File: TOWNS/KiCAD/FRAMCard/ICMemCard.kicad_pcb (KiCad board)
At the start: 2 copper layers, 79.1 x 50.5 mm, 17 parts, among them J1 PCMCIA_Connector, Q1 BC846X, Q2 BC846X, U1 FM18W08-SGTR, U2 FM18W08-SGTR

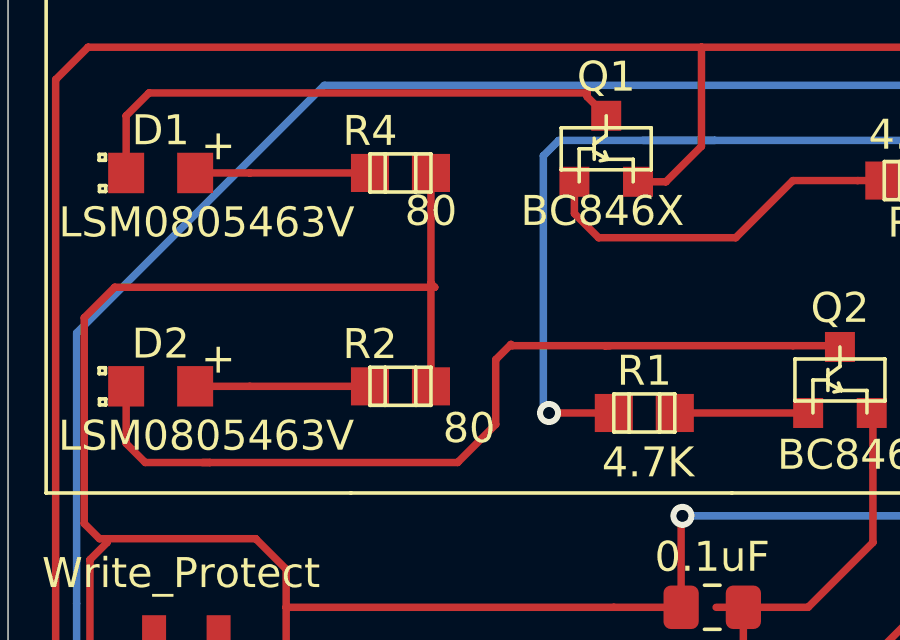
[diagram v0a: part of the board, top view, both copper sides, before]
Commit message: Updated resistance.
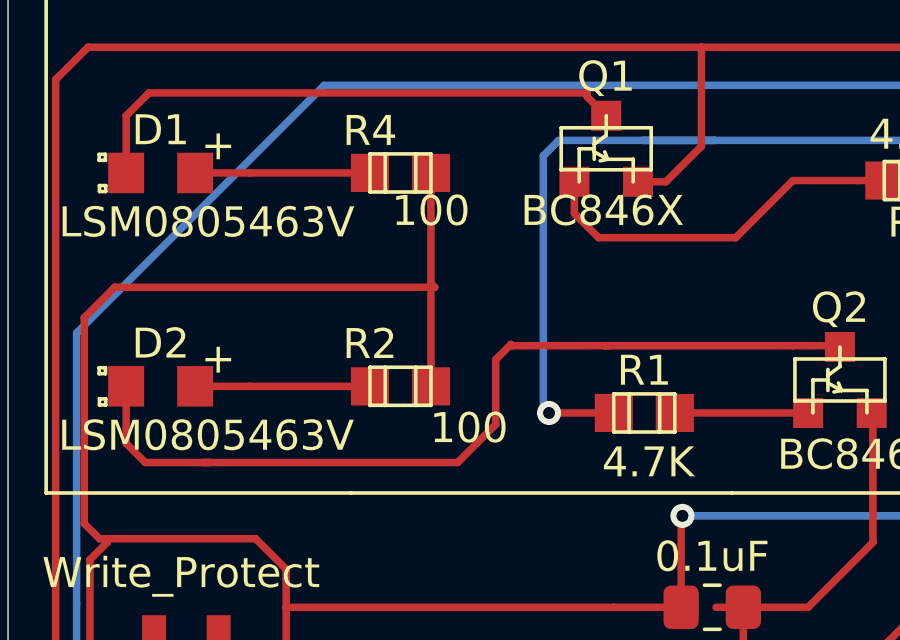
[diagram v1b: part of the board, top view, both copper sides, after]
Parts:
- R2, R4: value 80 -> 100

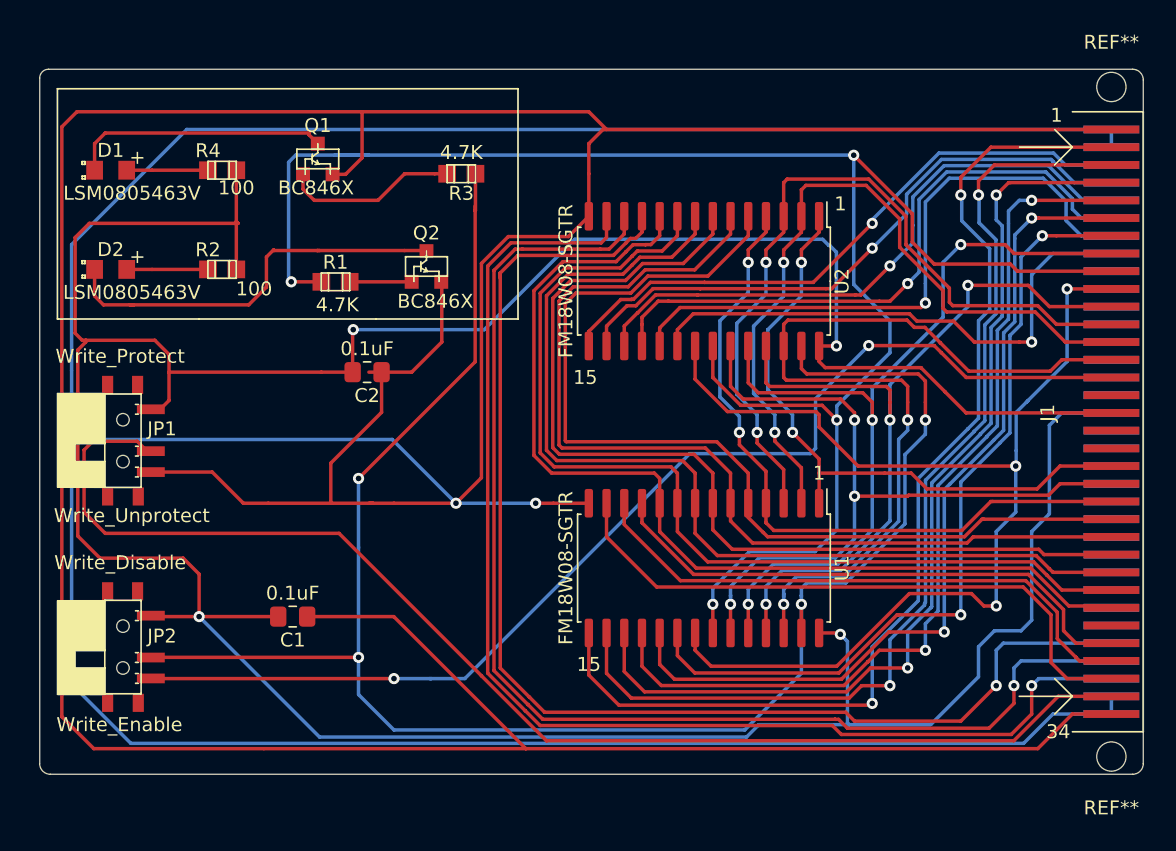
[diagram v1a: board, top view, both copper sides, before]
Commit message: Omitted ~WE switch.
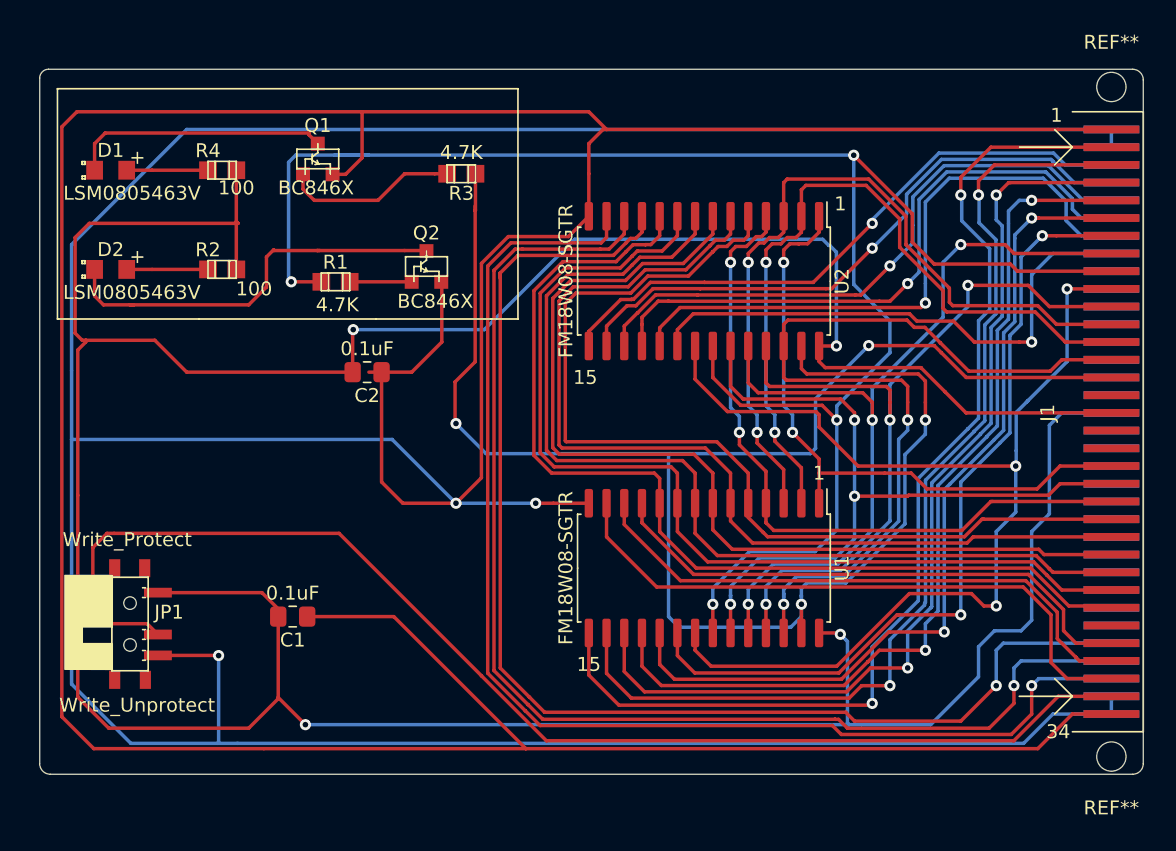
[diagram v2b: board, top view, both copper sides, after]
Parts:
- removed JP2: Write_Disable, PCMCIA:MA_Memory_Card_Slide_Switch
- moved JP1 13.2 mm to (68.7, 90.4)
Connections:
- J1 pad 15: /~WE_PC -> /~WE
- R3 pad 2: /~WE_IC -> /~WE
- U1 pad 27: /~WE_IC -> /~WE
- U2 pad 27: /~WE_IC -> /~WE
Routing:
- net /~WE: track 0.00 -> 130.4 mm, vias 0 -> 4
- net /~WE_IC: track 130.1 -> 0.00 mm, vias 4 -> 0
- net /~WE_PC: track 82.4 -> 0.00 mm, vias 2 -> 0
- net GND: track 528.1 -> 518.4 mm, vias 2 -> 3
- net Vcc: track 256.4 -> 263.9 mm
- net /Wp: track 91.3 -> 90.8 mm
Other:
- board text added: "FM TOWNS RESCUE BOOT MEMORY CARD by Captain YS http://www.ysflight.com Ver. 20220430"
- board text removed: "FM TOWNS RESCUE BOOT MEMORY CARD Ver. 20220429 by Captain YS http://www.ysflight.com"
- board text removed: "Write_Enable"

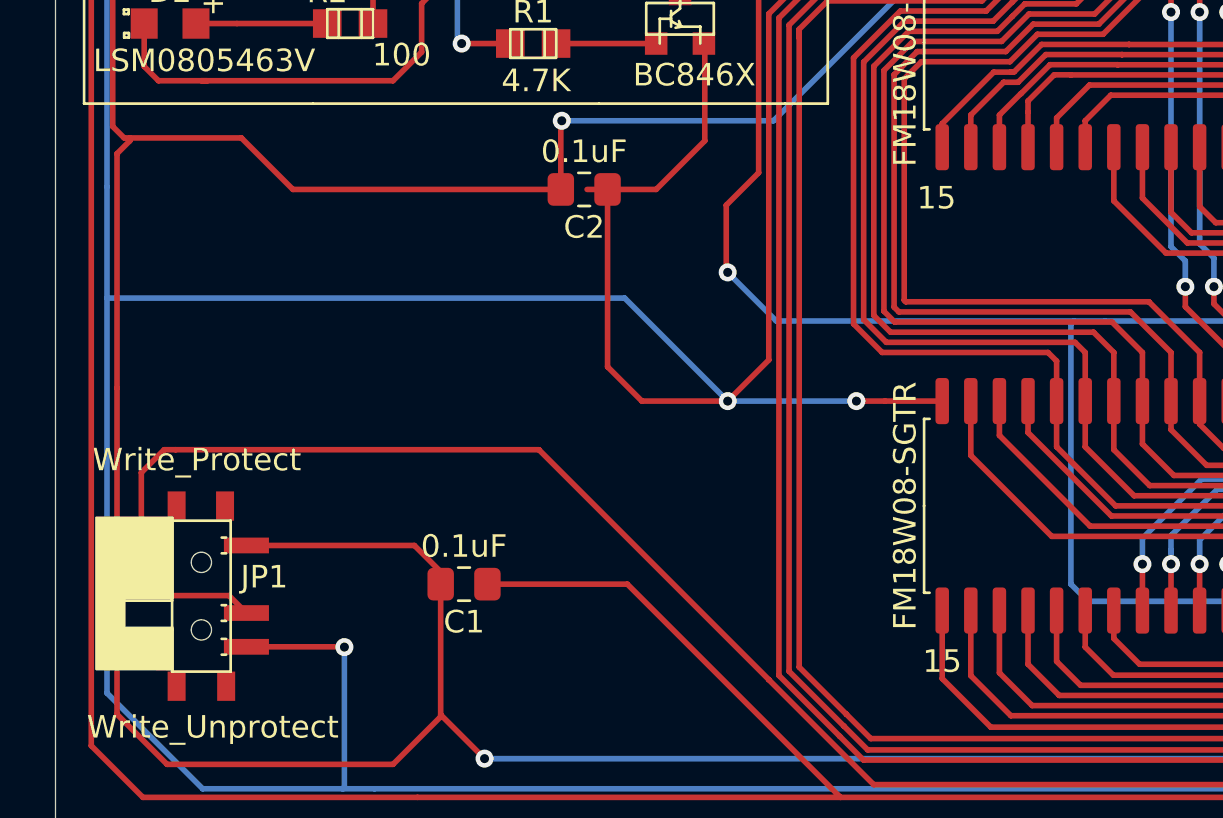
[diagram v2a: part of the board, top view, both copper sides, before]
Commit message: Updated FRAM card schematic and PCB.  Added pull-up resistors for ~CE1 and ~CE2 to prevent data corruption on hog-plug and hot-unplug.
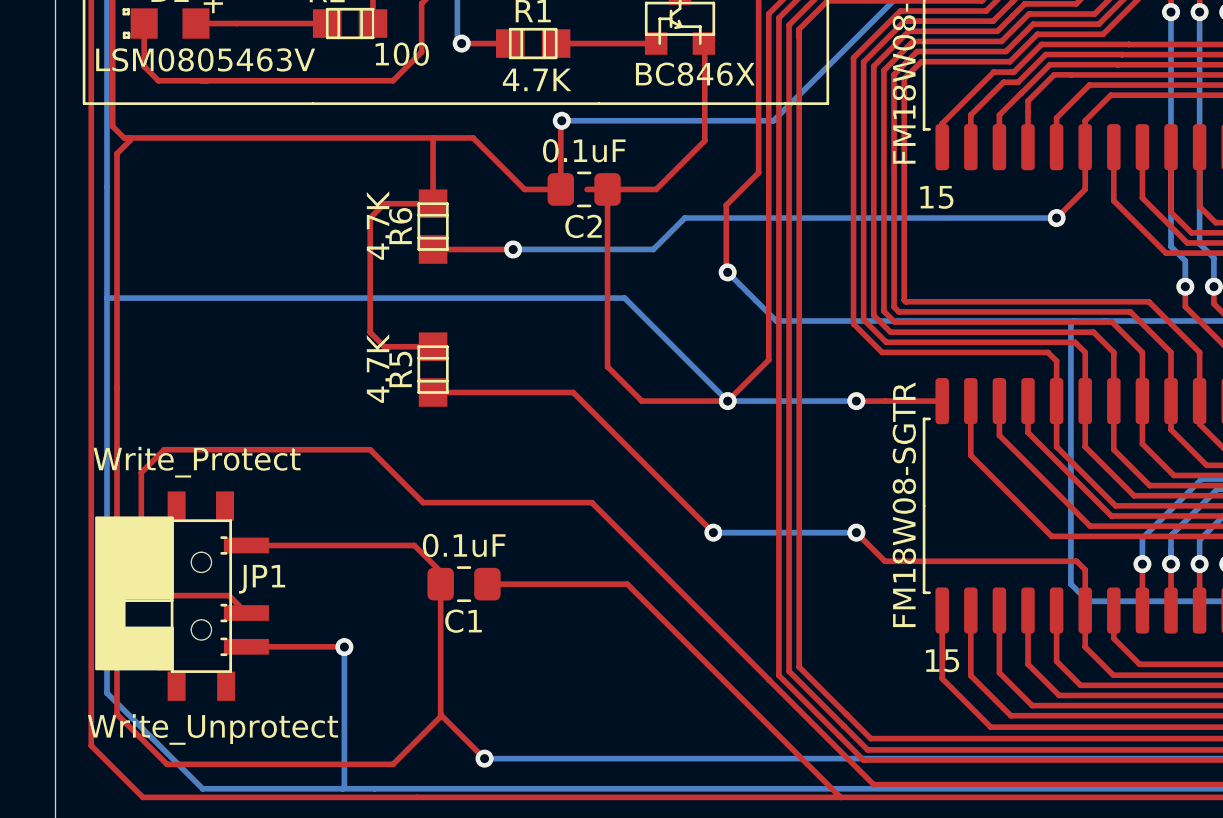
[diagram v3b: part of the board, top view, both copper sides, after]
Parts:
- added R5: 4.7K, PCMCIA:KOA_RK73G2AAT, F.Cu at (77.1, 80.4)
- added R6: 4.7K, PCMCIA:KOA_RK73G2AAT, F.Cu at (77.1, 74.0)
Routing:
- net /~CE1: track 58.7 -> 92.8 mm, vias 2 -> 4
- net /~CE2: track 39.1 -> 71.0 mm, vias 1 -> 3
- net Vcc: track 263.9 -> 278.0 mm
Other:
- board text added: "FM TOWNS RESCUE BOOT MEMORY CARD by Captain YS http://www.ysflight.com Ver. 20220510"
- board text removed: "FM TOWNS RESCUE BOOT MEMORY CARD by Captain YS http://www.ysflight.com Ver. 20220430"

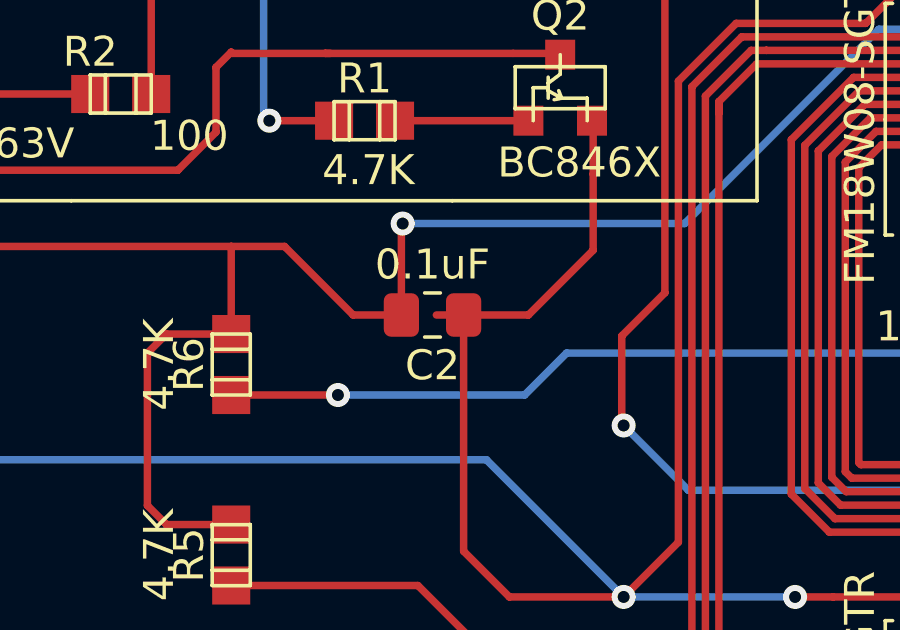
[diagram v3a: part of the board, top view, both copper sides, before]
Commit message: Fixed an artifact.
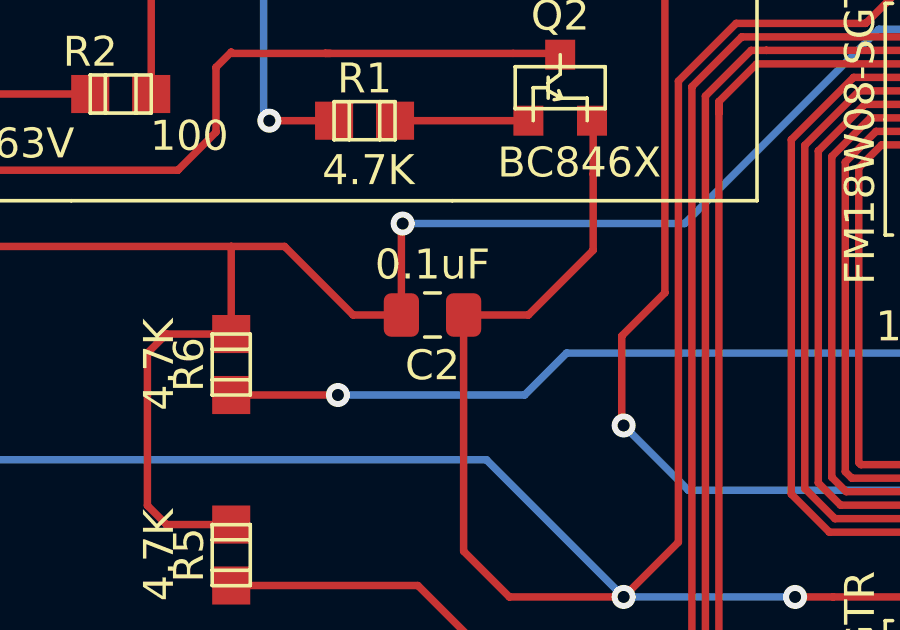
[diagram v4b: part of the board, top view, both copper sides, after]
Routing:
- net GND: track 518.4 -> 517.5 mm

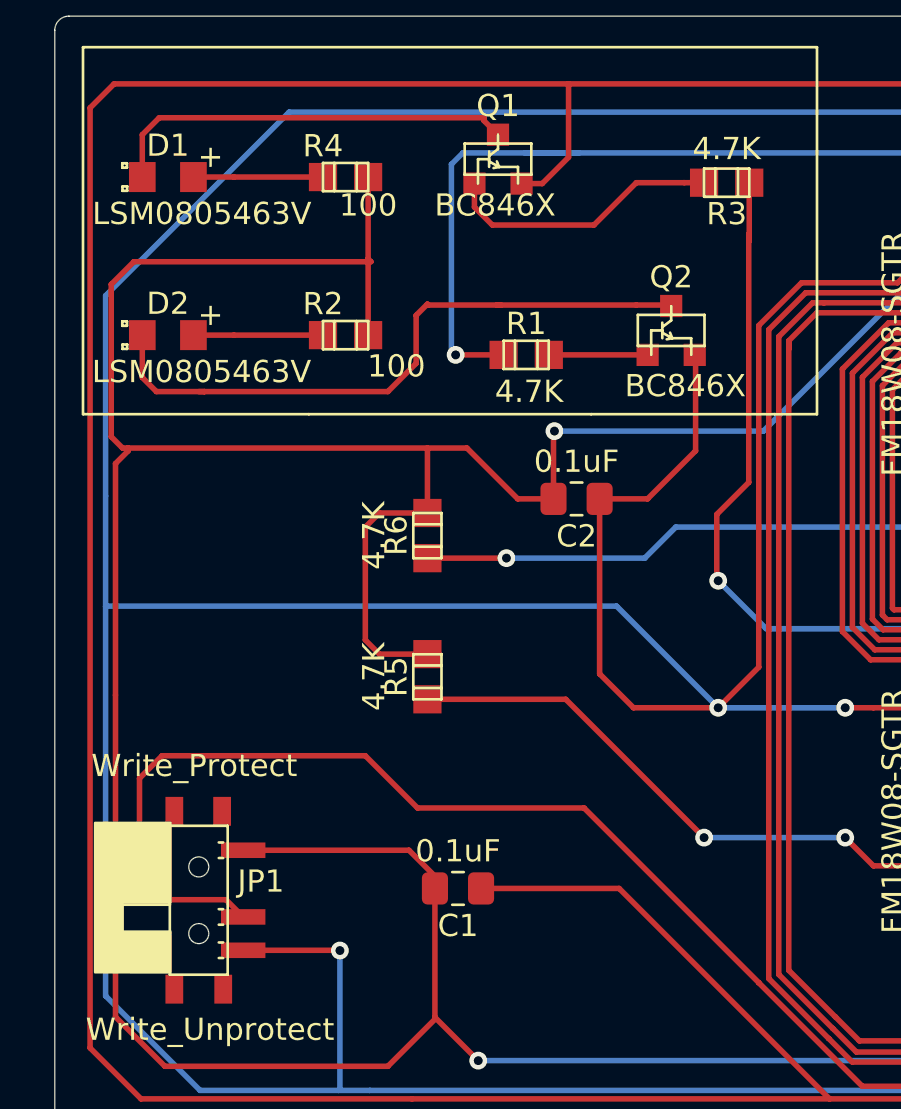
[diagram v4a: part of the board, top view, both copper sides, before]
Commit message: SOT353_Easy footprint.
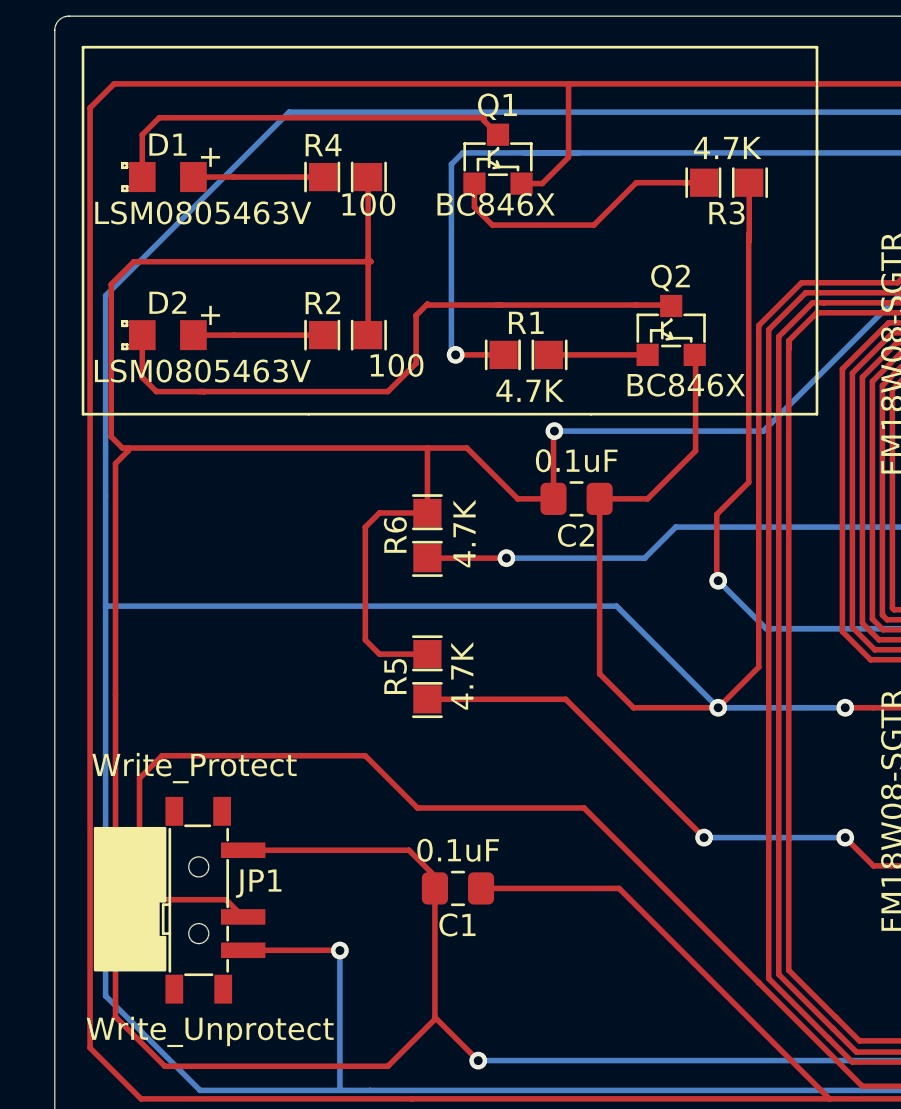
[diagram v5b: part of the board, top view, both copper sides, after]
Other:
- board text added: "FM TOWNS RESCUE BOOT MEMORY CARD by Captain YS http://www.ysflight.com Ver. 20220514"
- board text removed: "FM TOWNS RESCUE BOOT MEMORY CARD by Captain YS http://www.ysflight.com Ver. 20220510"
